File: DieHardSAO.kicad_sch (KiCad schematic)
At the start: 4 parts, among them X1 Badgelife_sao_connector_v169b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

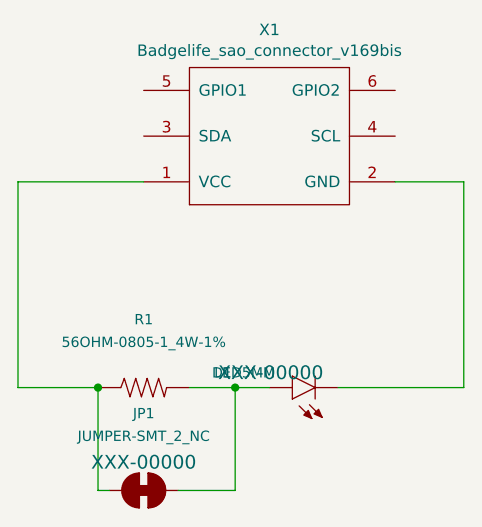
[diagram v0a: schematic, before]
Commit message: Changed jumper
Changed jumper and moved traces
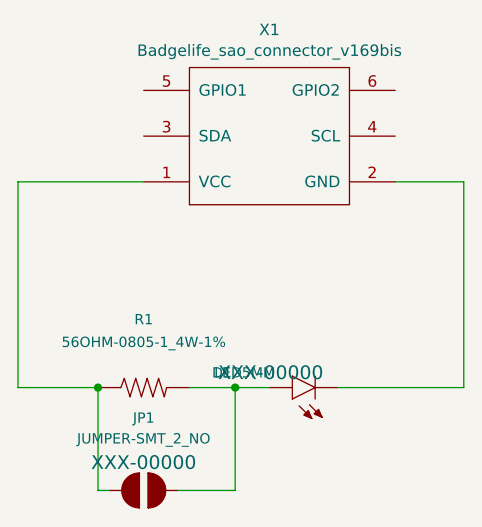
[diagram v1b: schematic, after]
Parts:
- removed JP1: JUMPER-SMT_2_NC, Jumpers:SMT-JUMPER_2_NC_TRACE_NO-SILK, symbol Sparkfun-Jumpers:JUMPER-SMT_2_NC
- added JP1: JUMPER-SMT_2_NO, SMT-JUMPER_2_NO, symbol Sparkfun-Jumpers:JUMPER-SMT_2_NO
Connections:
- net at R1.1, X1.1 (VCC): now also JP1.1
- net at D1.2 (A), R1.2: now also JP1.2
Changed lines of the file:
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@@
     (pin "6")
+  )
+  (symbol (lib_id "Sparkfun-Jumpers:JUMPER-SMT_2_NO") (at 125.73 115.57 0) (unit 1)
+    (in_bom yes) (on_board yes) (fields_autoplaced)
+    (property "Reference" "JP1" (id 0) (at 125.73 107.5131 0)
+      (effects (font (size 1.143 1.143)))
+    )
+    (property "Value" "JUMPER-SMT_2_NO" (id 1) (at 125.73 109.8217 0)
+      (effects (font (size 1.143 1.143)))
+    )
+    (property "Footprint" "SMT-JUMPER_2_NO" (id 2) (at 125.73 110.49 0)
+      (effects (font (size 0.508 0.508)) hide)
+    )
+    (property "Datasheet" "" (id 3) (at 125.73 115.57 0)
+      (effects (font (size 1.524 1.524)) hide)
+    )
+    (property "PROD_ID" "XXX-00000" (id 4) (at 125.73 112.4727 0)
+      (effects (font (size 1.524 1.524)))
+    )
+    (pin "1")
+    (pin "2")
   )
   (symbol (lib_id "SparkFun-LED:LED5MM") (at 142.24 104.14 90) (unit 1)
@@
     )
     (property "Field4" "XXX-00000" (id 4) (at 139.8451 102.489 90)
-      (effects (font (size 1.524 1.524)))
-    )
-    (pin "1")
-    (pin "2")
-  )
-  (symbol (lib_id "Sparkfun-Jumpers:JUMPER-SMT_2_NC") (at 125.73 115.57 0) (unit 1)
-    (in_bom yes) (on_board yes) (fields_autoplaced)
-    (property "Reference" "JP1" (id 0) (at 125.73 107.0148 0)
-      (effects (font (size 1.143 1.143)))
-    )
-    (property "Value" "JUMPER-SMT_2_NC" (id 1) (at 125.73 109.5376 0)
-      (effects (font (size 1.143 1.143)))
-    )
-    (property "Footprint" "Jumpers:SMT-JUMPER_2_NC_TRACE_NO-SILK" (id 2) (at 125.73 110.49 0)
-      (effects (font (size 0.508 0.508)) hide)
-    )
-    (property "Datasheet" "" (id 3) (at 125.73 115.57 0)
-      (effects (font (size 1.524 1.524)) hide)
-    )
-    (property "PROD_ID" "XXX-00000" (id 4) (at 125.73 112.4385 0)
       (effects (font (size 1.524 1.524)))
     )
@@
       (reference "D1") (unit 1) (value "LED5MM") (footprint "LED_THT:LED_D5.0mm_Horizontal_O3.81mm_Z9.0mm")
     )
-    (path "/52fe3400-bf18-4fe5-aa6e-2be779b65697"
-      (reference "JP1") (unit 1) (value "JUMPER-SMT_2_NC") (footprint "Jumpers:SMT-JUMPER_2_NC_TRACE_NO-SILK")
+    (path "/45060941-0985-476d-88eb-2ef2eab2f4c7"
+      (reference "JP1") (unit 1) (value "JUMPER-SMT_2_NO") (footprint "SMT-JUMPER_2_NO")
     )
     (path "/b5d24432-2e11-4323-8d9e-7a51fa3b8345"

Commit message: Changed jumper footprint and clean up
Changed the jumper footprint.

Cleaned up auto generated files and added them to the ignore list.

Change the gerber file output directory from Output/v2 to Output
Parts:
- JP1: footprint SMT-JUMPER_2_NO -> Jumper:SolderJumper-2_P1.3mm_Open_TrianglePad1.0x1.5mm
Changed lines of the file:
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@@
       (effects (font (size 1.143 1.143)))
     )
-    (property "Footprint" "SMT-JUMPER_2_NO" (id 2) (at 125.73 110.49 0)
+    (property "Footprint" "Jumper:SolderJumper-2_P1.3mm_Open_TrianglePad1.0x1.5mm" (id 2) (at 125.73 110.49 0)
       (effects (font (size 0.508 0.508)) hide)
     )
@@
     )
     (path "/45060941-0985-476d-88eb-2ef2eab2f4c7"
-      (reference "JP1") (unit 1) (value "JUMPER-SMT_2_NO") (footprint "SMT-JUMPER_2_NO")
+      (reference "JP1") (unit 1) (value "JUMPER-SMT_2_NO") (footprint "Jumper:SolderJumper-2_P1.3mm_Open_TrianglePad1.0x1.5mm")
     )
     (path "/b5d24432-2e11-4323-8d9e-7a51fa3b8345"
